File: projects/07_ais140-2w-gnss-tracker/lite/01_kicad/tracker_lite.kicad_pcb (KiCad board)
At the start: 2 copper layers, 60 x 45 mm, 113 parts, among them J1 VEHICLE 4P, J2 LiPo 300mAh, J4 LTE ANT, J5 GNSS ANT, Q1 AO3401A, Q2 2N7002, Q3 BSS138, Q4 BSS138, Q5 MMBT3904, Q6 AO3400A, Q7 MMBT3904, Q8 MMBT3904, U1 XL1509-ADJ, U2 MCP73831-2, U3 EC200U-CN, U5 L76K, U6 AP2112K-3.3, U7 LIS3DH, U8 MFF2 eSIM

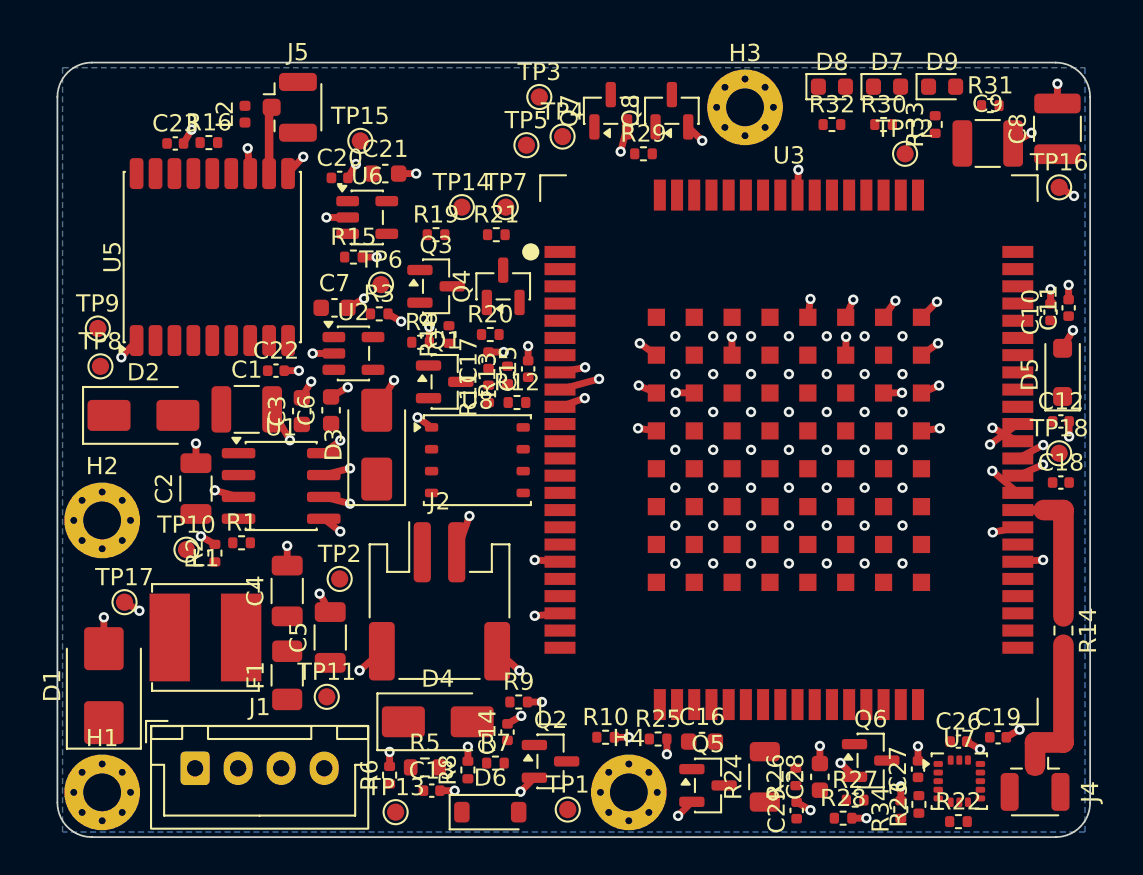
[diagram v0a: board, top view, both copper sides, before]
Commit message: Tracker 07 Lite (WIP): 50 ohm LTE CPWG, U.FL side entry, routable power classes
Co-Authored-By: Claude Opus 5.5 <noreply@anthropic.com>
Claude-Session: https://claude.ai/code/session_01Hk6s8R6up8HYVQWXd3atVk
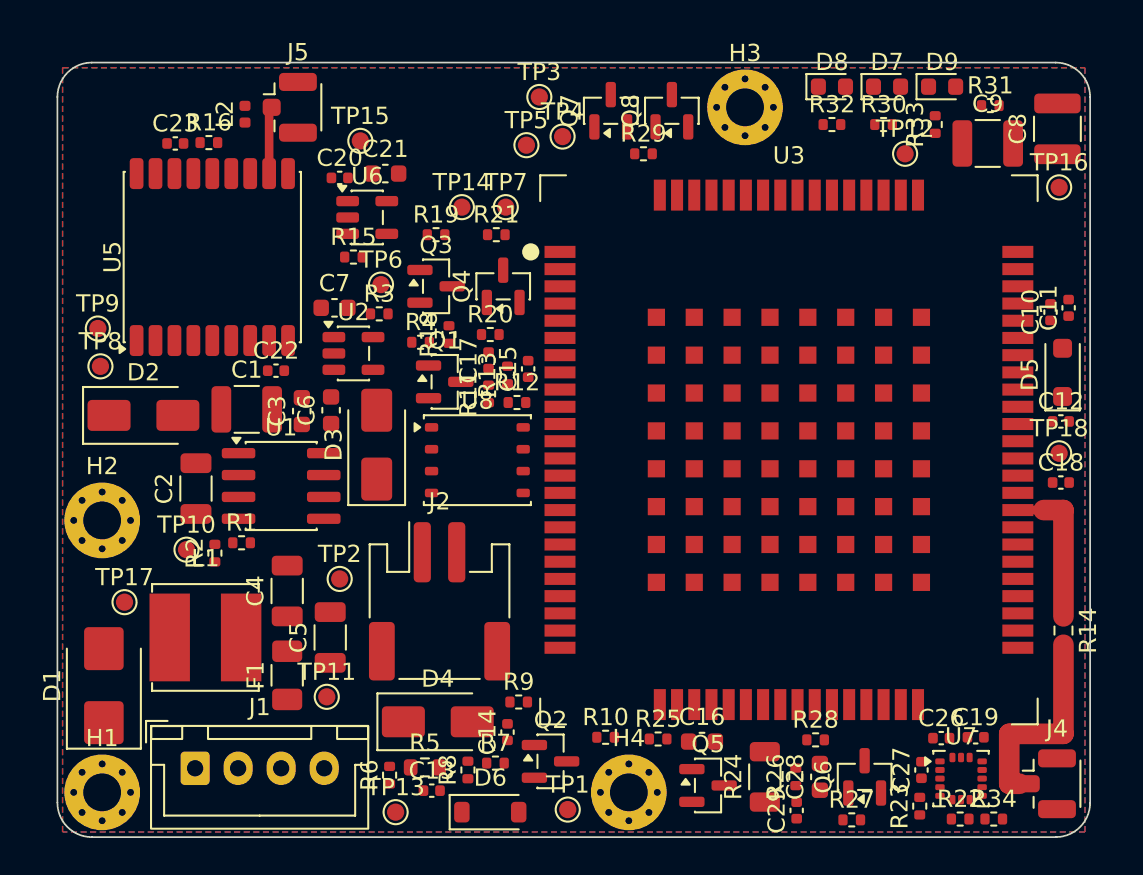
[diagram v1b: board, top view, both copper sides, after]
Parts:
- moved R34 5.43 mm to (154.4, 143.9), turned to 0 degrees
- moved R28 4.82 mm to (144.1, 139.3)
- moved C19 1.30 mm to (153.3, 139.2)
- moved R27 1.17 mm to (146.2, 144.0)
- moved C26 1.02 mm to (151.3, 139.2)
- moved Q6 1.01 mm to (146.9, 141.5), turned to 90 degrees
- moved J4 0.80 mm to (157.6, 141.9), turned to 0 degrees
- moved C27 0.21 mm to (150.2, 141.1)
- moved R22 0.18 mm to (152.4, 143.9)
- moved U7 0.18 mm to (152.5, 141.6)
- moved R23 0.11 mm to (150.1, 143.2)
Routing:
- net GND: track 105.8 -> 0.00 mm, vias 136 -> 0
- net LTE_RF: track 8.68 -> 12.5 mm
- added copper zone on F.Cu, net GND

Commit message: Tracker 07 Lite (WIP): L-match LTE, passive GNSS patch, bottom test pads, fab script
Co-Authored-By: Claude Opus 5.5 <noreply@anthropic.com>
Claude-Session: https://claude.ai/code/session_01Hk6s8R6up8HYVQWXd3atVk
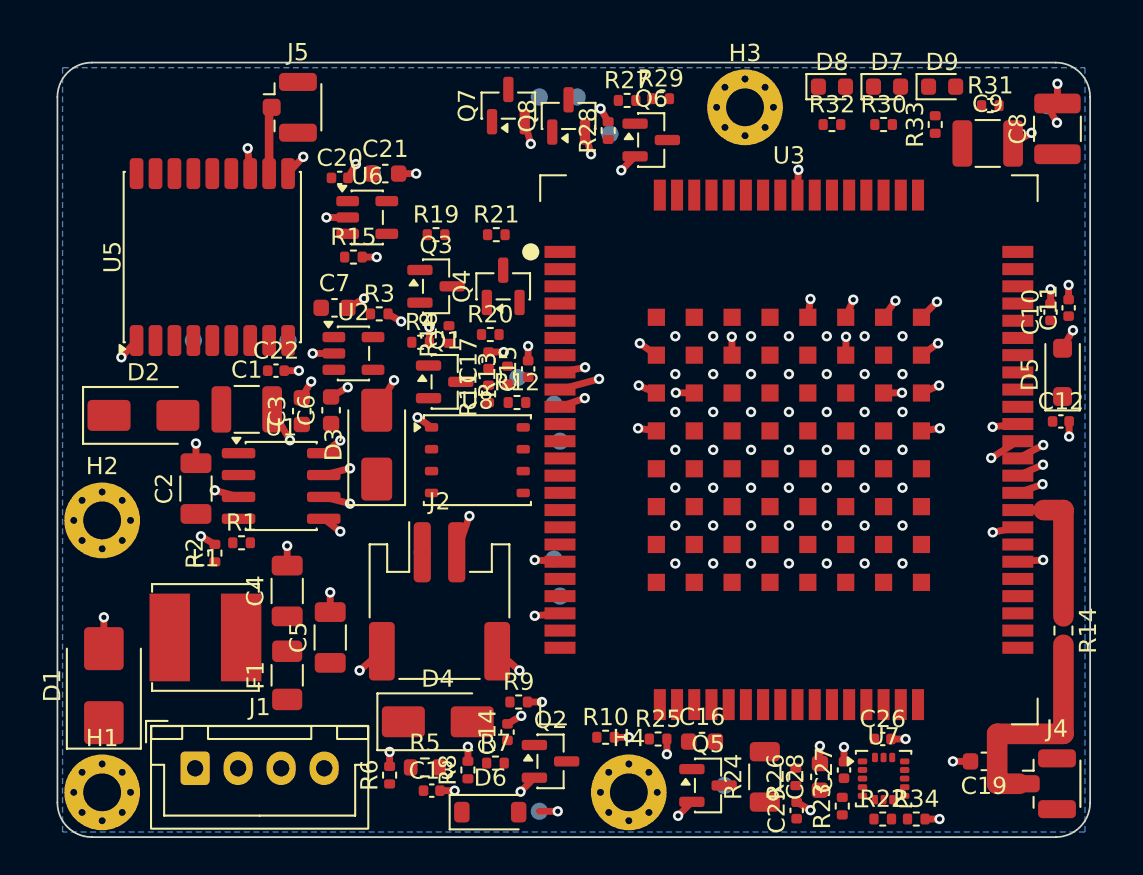
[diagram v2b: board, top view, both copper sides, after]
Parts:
- removed C18: DNP, Capacitor_SMD:C_0402_1005Metric
- removed C23: 10nF, Capacitor_SMD:C_0402_1005Metric
- removed L2: 47nH, Inductor_SMD:L_0402_1005Metric
- removed R16: 10R, Resistor_SMD:R_0402_1005Metric
- C19: footprint Capacitor_SMD:C_0402_1005Metric -> Capacitor_SMD:C_0603_1608Metric
- TP1, TP10, TP11, TP12, TP13, TP14, TP15, TP16, TP17, TP18, TP2, TP3, TP4, TP5, TP6, TP7, TP8, TP9: moved to B.Cu
- moved R27 43.8 mm to (133.1, 102.2)
- moved Q6 39.0 mm to (134.5, 104.5), turned to 0 degrees
- moved R28 37.4 mm to (132.0, 104.0), turned to 90 degrees
- moved TP18 27.4 mm to (138.8, 142.0)
- moved TP17 27.0 mm to (128.0, 143.5)
- moved TP13 15.2 mm to (121.2, 128.4)
- moved TP6 13.8 mm to (129.2, 122.0)
- moved TP2 12.5 mm to (128.8, 128.8)
- moved TP1 12.4 mm to (129.2, 131.0)
- moved TP7 11.8 mm to (128.8, 119.8)
- moved TP8 11.0 mm to (113.4, 116.2)
- moved TP14 10.4 mm to (126.8, 118.3)
- moved TP10 8.40 mm to (109.5, 120.2)
- moved Q8 6.01 mm to (129.7, 103.1)
- moved Q7 5.96 mm to (126.2, 102.5)
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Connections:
- U5 pad 14: GNSS_VCC_RF -> unconnected-(U5-VCC_RF-Pad14)
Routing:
- net GND: track 0.00 -> 104.4 mm, vias 0 -> 135
- net LTE_RF: track 12.5 -> 13.9 mm
- removed copper zone on F.Cu, net GND

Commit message: Tracker 07 Lite: routed 2-layer PCB, fab outputs, costed BOM, 3D and docs
CRL-TRK-2W-L1 (EC200U-CN Cat-1/GSM + L76K + LIS3DH), 60x45 mm, single-sided SMT.
ERC 0, DRC 0 errors / 0 unconnected, parity clean. Gerbers, JLC BOM/CPL, STEP,
renders, design report, verify list (EC200U land pattern must be replaced
with the Quectel drawing before fab). Hardware ~Rs 1,440 @1k.

Co-Authored-By: Claude Opus 5.5 <noreply@anthropic.com>
Claude-Session: https://claude.ai/code/session_01Hk6s8R6up8HYVQWXd3atVk
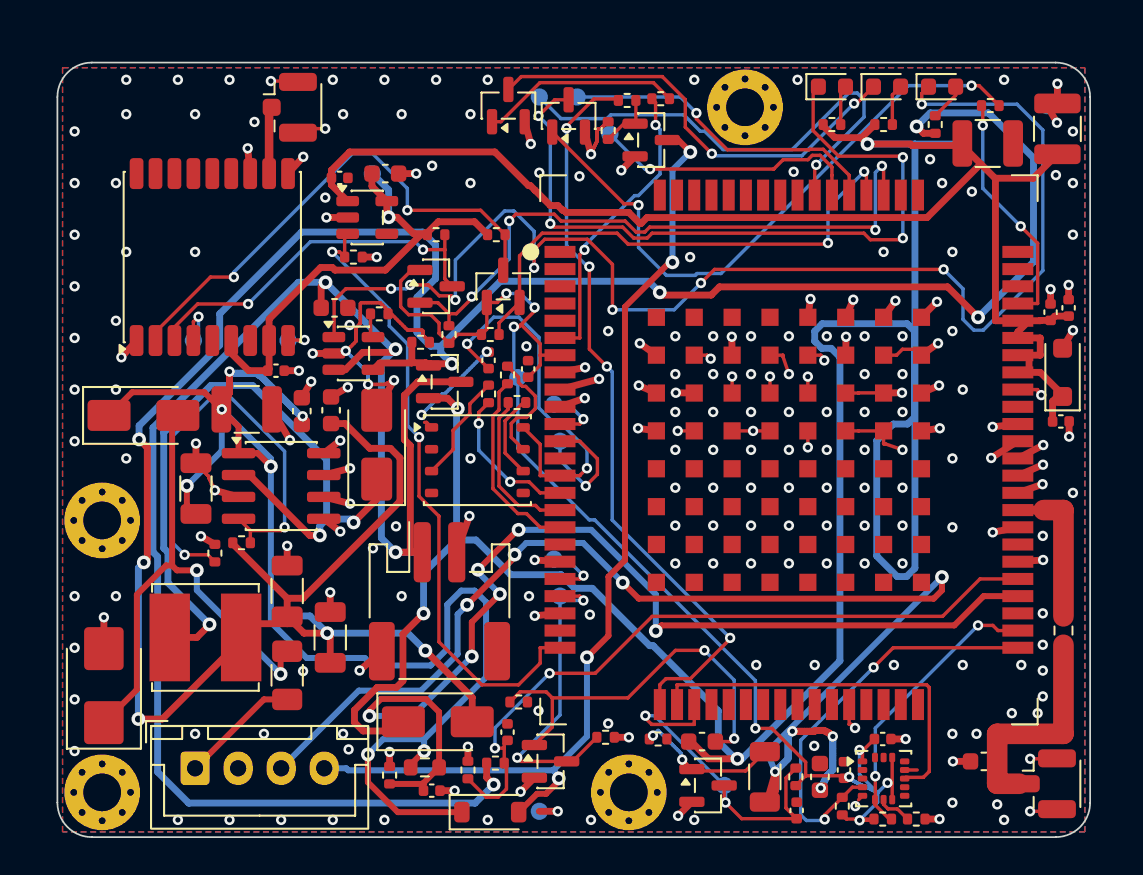
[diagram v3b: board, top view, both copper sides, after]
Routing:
- net VSYS: track 0.00 -> 218.3 mm, vias 0 -> 4
- net V4_BUCK: track 0.00 -> 161.3 mm, vias 0 -> 9
- net VBAT: track 0.00 -> 95.5 mm, vias 0 -> 4
- net VIN_PROT: track 0.00 -> 81.5 mm, vias 0 -> 7
- net CHG_STAT: track 0.00 -> 76.6 mm, vias 0 -> 8
- net IGN_RAW: track 0.00 -> 75.6 mm, vias 0 -> 8
- net MDM_1V8: track 0.00 -> 73.6 mm, vias 0 -> 8
- net VIN_SENSE: track 0.00 -> 62.3 mm, vias 0 -> 6
- net RELAY_OUT: track 0.00 -> 58.1 mm, vias 0 -> 4
- net RELAY_CTL: track 0.00 -> 43.8 mm, vias 0 -> 4
- net LED_PWR_K: track 0.00 -> 43.1 mm, vias 0 -> 4
- net BUCK_SW: track 0.00 -> 42.7 mm, vias 0 -> 3
- net VBAT_SENSE: track 0.00 -> 41.5 mm, vias 0 -> 2
- net MDM_TX_1V8: track 0.00 -> 37.4 mm, vias 0 -> 4
- net GNSS_EN: track 0.00 -> 37.0 mm, vias 0 -> 2
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- added copper zone on F.Cu, net GND
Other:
- board text added: "CRL-TRK-2W-L1 A0"
- board text added: "Samay Track 2W Lite"
